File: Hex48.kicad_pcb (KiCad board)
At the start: 2 copper layers, 78 x 90.5 mm, 43 parts, among them J1 Conn_02x24_Counter_Clockwise, J2 Conn_02x24_Odd_Even, J3 Conn_02x24_Odd_Even, J4 Conn_02x02_Odd_Even, J5 Conn_02x02_Odd_Even, J6 Conn_02x24_Odd_Even, J7 Conn_02x12_Counter_Clockwise, J8 Conn_02x12_Counter_Clockwise, SW1 SW_Push, SW2 SW_Push

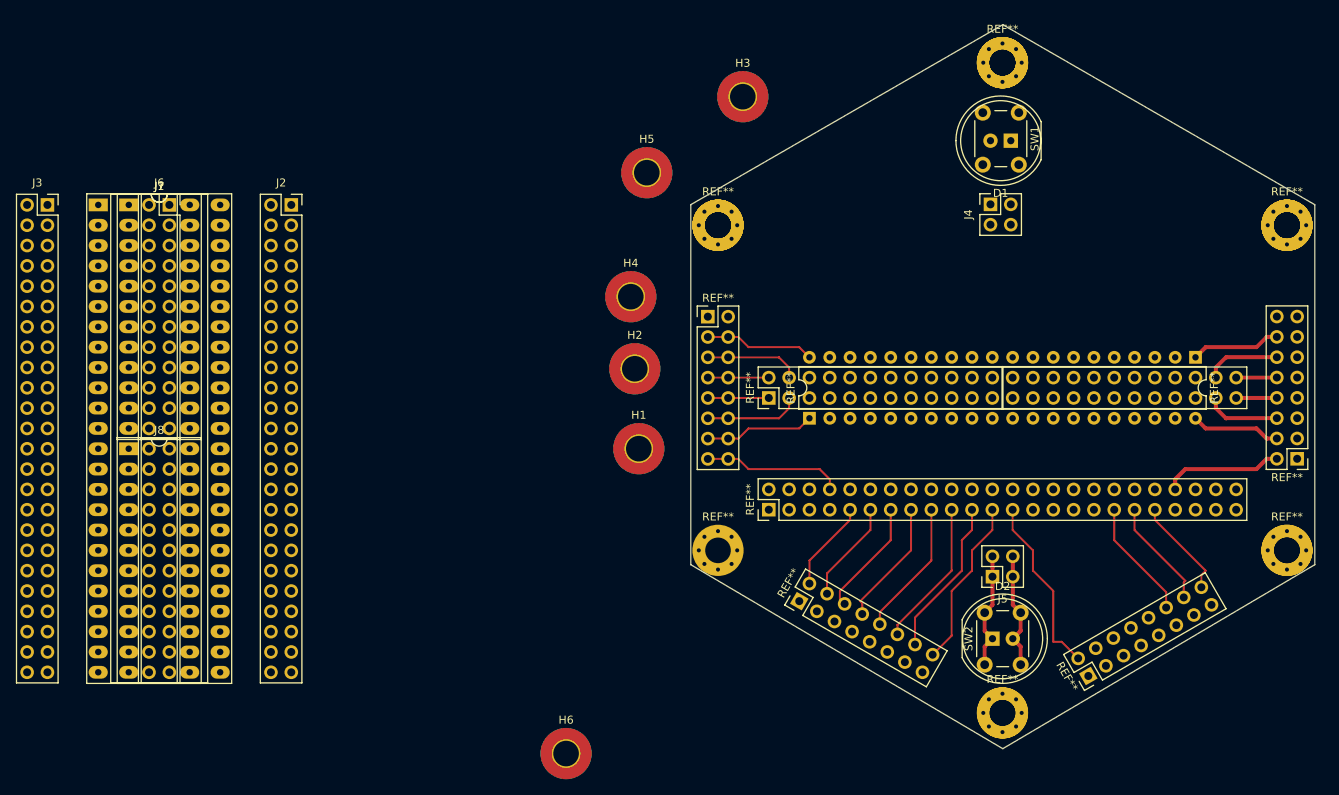
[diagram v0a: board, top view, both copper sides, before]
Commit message: Finish schematic, map all footprints,update PCB.
Rats-nest now complete. Some parts placed on PCB in final locations. Some parts (mounting holes and 2x8 headers) need to be placed exactly on a polar grid at 60-degree intervals.
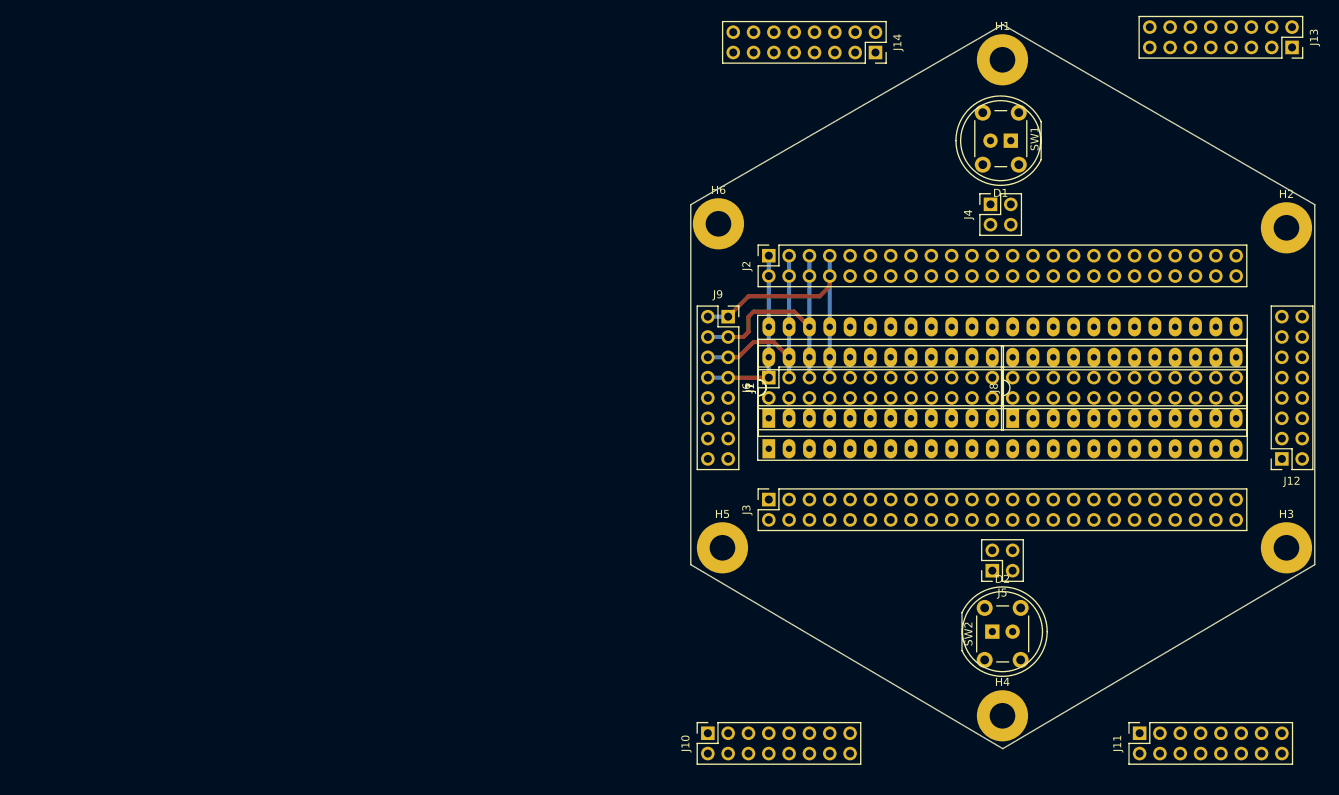
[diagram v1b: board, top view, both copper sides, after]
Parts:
- removed ? (x11): , 
- removed REF** (x6): MountingHole_3.2mm_M3_Pad_Via, MountingHole:MountingHole_3.2mm_M3_Pad_Via
- removed REF** (x4): PinHeader_2x08_P2.54mm_Vertical, Connector_PinHeader_2.54mm:PinHeader_2x08_P2.54mm_Vertical
- removed REF** (x2): DIP-20_W7.62mm, Package_DIP:DIP-20_W7.62mm
- removed REF** (x2): PinHeader_2x24_P2.54mm_Vertical, Connector_PinHeader_2.54mm:PinHeader_2x24_P2.54mm_Vertical
- added J10: Conn_02x08_Odd_Even, Connector_PinSocket_2.54mm:PinSocket_2x08_P2.54mm_Vertical, F.Cu at (151.1, 115.6)
- added J11: Conn_02x08_Odd_Even, Connector_PinSocket_2.54mm:PinSocket_2x08_P2.54mm_Vertical, F.Cu at (205.1, 115.6)
- added J12: Conn_02x08_Odd_Even, Connector_PinSocket_2.54mm:PinSocket_2x08_P2.54mm_Vertical, F.Cu at (222.9, 81.3)
- added J13: Conn_02x08_Odd_Even, Connector_PinSocket_2.54mm:PinSocket_2x08_P2.54mm_Vertical, F.Cu at (224.2, 29.8)
- added J14: Conn_02x08_Odd_Even, Connector_PinSocket_2.54mm:PinSocket_2x08_P2.54mm_Vertical, F.Cu at (172.1, 30.5)
- added J9: Conn_02x08_Odd_Even, Connector_PinSocket_2.54mm:PinSocket_2x08_P2.54mm_Vertical, F.Cu at (153.7, 63.5)
- H1, H2, H3, H4, H5, H6: footprint MountingHole:MountingHole_3.2mm_M3_Pad_TopBottom -> MountingHole:MountingHole_3.2mm_M3_Pad
- moved J8 110.6 mm to (189.2, 76.2), turned to 90 degrees
- moved J3 97.4 mm to (158.8, 86.4), turned to 90 degrees
- moved J1 89.2 mm to (158.8, 80.0), turned to 90 degrees
- moved H3 88.3 mm to (223.5, 92.4)
- moved J7 84.3 mm to (158.7, 76.2), turned to 90 degrees
- moved H2 83.3 mm to (223.5, 52.4)
- moved J6 78.0 mm to (158.8, 71.1), turned to 90 degrees
- moved H4 70.0 mm to (188.0, 113.4)
- moved H6 68.9 mm to (152.5, 51.9)
- moved H1 66.6 mm to (188.0, 31.4)
- moved J2 60.0 mm to (158.8, 55.9), turned to 90 degrees
- moved H5 47.8 mm to (153.0, 92.4)
- moved D2 0.88 mm to (186.7, 102.9)
- moved J5 0.75 mm to (186.7, 95.2)
- moved SW2 0.59 mm to (185.7, 106.4)
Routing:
- net (no net): track 302.2 -> 0.00 mm
- net Net-(D2-A): track 58.6 -> 0.00 mm
- net /pin45: track 0.00 -> 33.3 mm
- net /pin46: track 0.00 -> 31.2 mm
- net /pin47: track 0.00 -> 27.0 mm
- net /pin48: track 0.00 -> 22.9 mm
- net Net-(D2-K): track 15.8 -> 0.00 mm

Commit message: Place footprints on PCB in exact locations.
PCB edges, mounting holes, connectors, and LEDs/switches in correct places. Footprints locked to avoid mistakes. Initial rear copper tracks added. Dimensions of hexagon and mounting holes added. TODO: lots more tack routing.
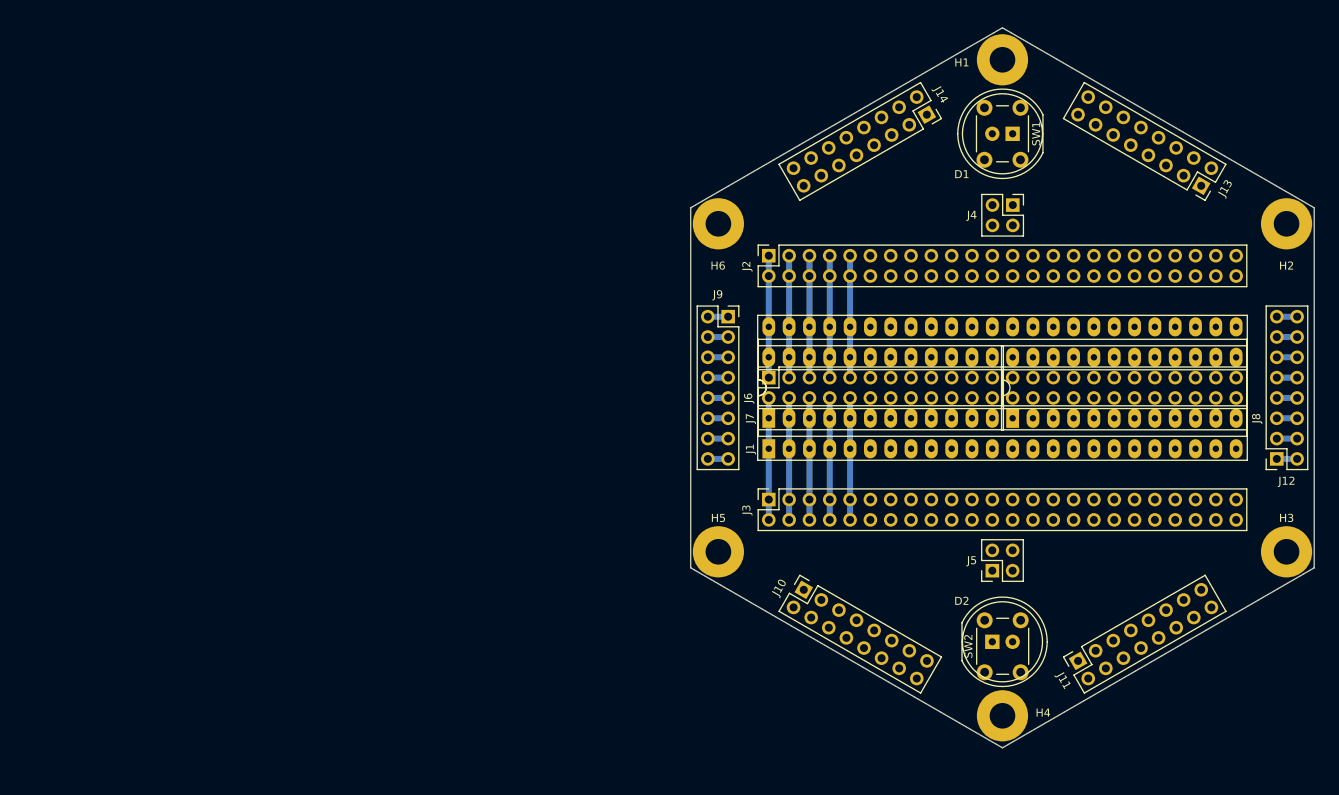
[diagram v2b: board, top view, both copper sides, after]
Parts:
- moved J10 21.6 mm to (163.1, 97.6), turned to 60 degrees
- moved J13 20.7 mm to (212.8, 47.1), turned to -120 degrees
- moved J11 11.9 mm to (197.4, 106.5), turned to 120 degrees
- moved J14 10.1 mm to (178.5, 38.2), turned to -60 degrees
- moved J4 2.79 mm to (189.2, 49.5), turned to 0 degrees
- moved SW2 1.55 mm to (185.7, 108.0)
- moved D2 1.27 mm to (186.7, 104.1)
- moved D1 0.89 mm to (189.2, 40.6)
- moved H5 0.71 mm to (152.4, 92.9)
- moved SW1 0.65 mm to (190.2, 37.4)
- moved J12 0.63 mm to (222.2, 81.3)
- moved H2 0.50 mm to (223.5, 51.9)
- moved H3 0.50 mm to (223.5, 92.9)
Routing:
- net /pin3: track 0.00 -> 17.8 mm
- net /pin4: track 0.00 -> 17.8 mm
- net /pin2: track 0.00 -> 17.8 mm
- net /pin1: track 0.00 -> 17.8 mm
- net /pin45: track 33.3 -> 17.8 mm
- net /pin5: track 0.00 -> 15.2 mm
- net /pin44: track 0.00 -> 15.2 mm
- net /pin46: track 31.2 -> 17.8 mm
- net /pin47: track 27.0 -> 17.8 mm
- net /pin48: track 22.9 -> 17.8 mm
- net /pin28: track 0.00 -> 2.54 mm
- net /pin27: track 0.00 -> 2.54 mm
- net /pin26: track 0.00 -> 2.54 mm
- net /pin25: track 0.00 -> 2.54 mm
- net /pin24: track 0.00 -> 2.54 mm
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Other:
- board size 78 x 90.5 mm -> 77.9 x 90 mm

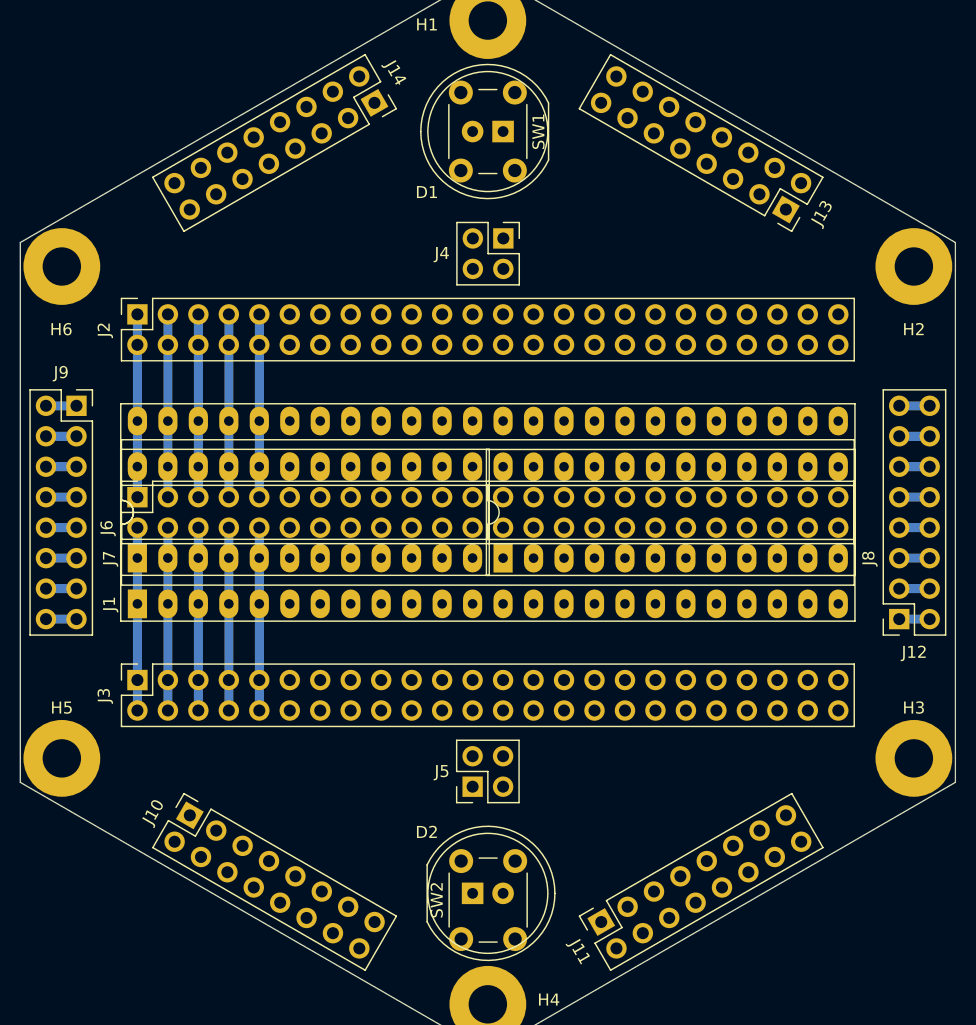
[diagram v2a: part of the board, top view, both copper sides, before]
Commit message: Route all tracks.
Try to put tracks on top where they will be visible and self-documenting. Tracks at 45 degrees under 60-degree mounted headers look a bit odd, but they work. All tracks 0.75mm wide. Some spacings a bit tight, may move.
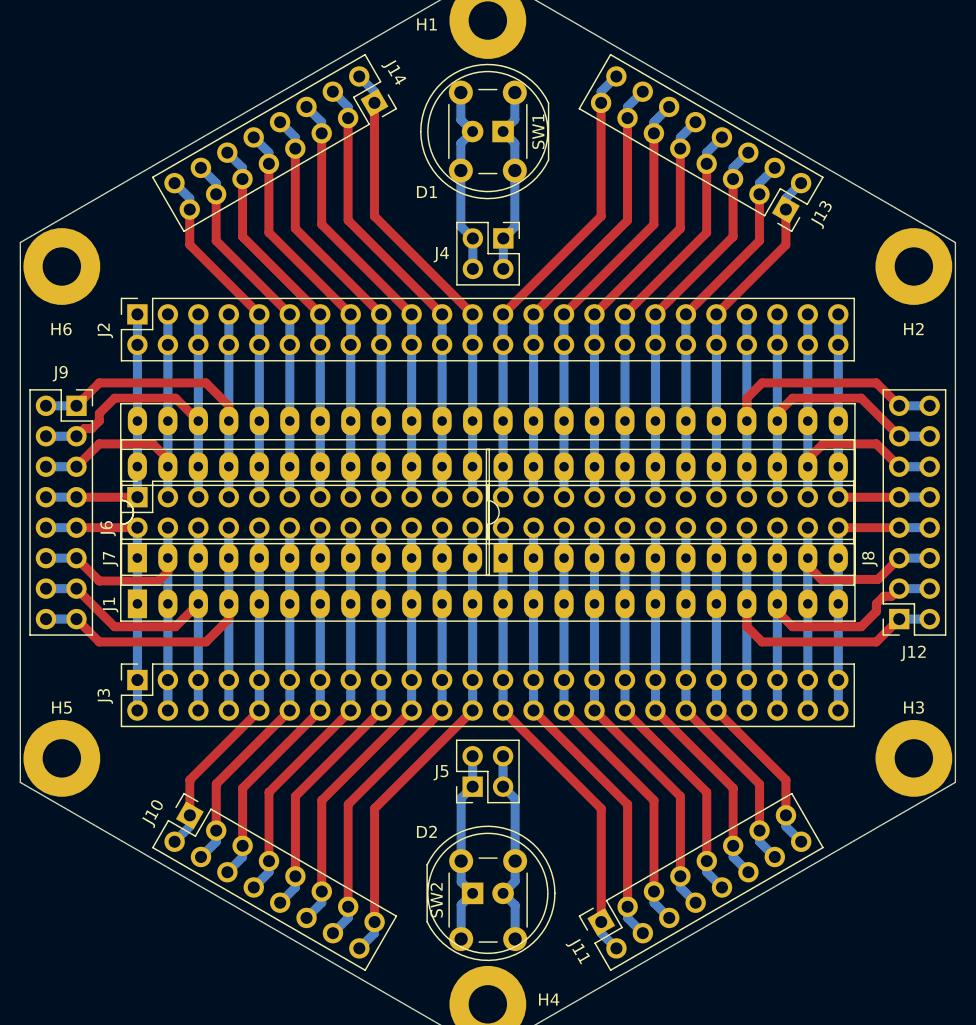
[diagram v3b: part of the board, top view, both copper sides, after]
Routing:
- net /pin13: track 0.00 -> 39.0 mm
- net /pin37: track 0.00 -> 39.0 mm
- net /pin36: track 0.00 -> 39.0 mm
- net /pin12: track 0.00 -> 39.0 mm
- net /pin14: track 0.00 -> 37.6 mm
- net /pin38: track 0.00 -> 37.6 mm
- net /pin35: track 0.00 -> 37.6 mm
- net /pin11: track 0.00 -> 37.6 mm
- net /pin39: track 0.00 -> 36.2 mm
- net /pin15: track 0.00 -> 36.2 mm
- net /pin10: track 0.00 -> 36.2 mm
- net /pin34: track 0.00 -> 36.2 mm
- net /pin16: track 0.00 -> 34.8 mm
- net /pin40: track 0.00 -> 34.8 mm
- net /pin33: track 0.00 -> 34.8 mm
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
